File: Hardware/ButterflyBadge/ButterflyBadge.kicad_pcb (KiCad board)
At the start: 4 copper layers, 26.7 x 96.5 mm, 98 parts, among them J1 USB_C_Receptacle_USB2.0, J4 Conn_02x07_Odd_Even, M1 Motor_DC, P1 TC2030-CTX, Q1 ALS-PT19, Q2 Q_NMOS_GSD, SW1 SW_Push, SW3 SW_SPDT, U1 W25Q128JVS, U2 CN3058, U25 AP3722AT, U3 RP2040, U4 AX5201, U5 AMS1117-3.3, U6 Si24R1, U7 TFDU4301, U8 SM351LT, U9 TMI8118, Y1 12MHz, Y2 16MHz

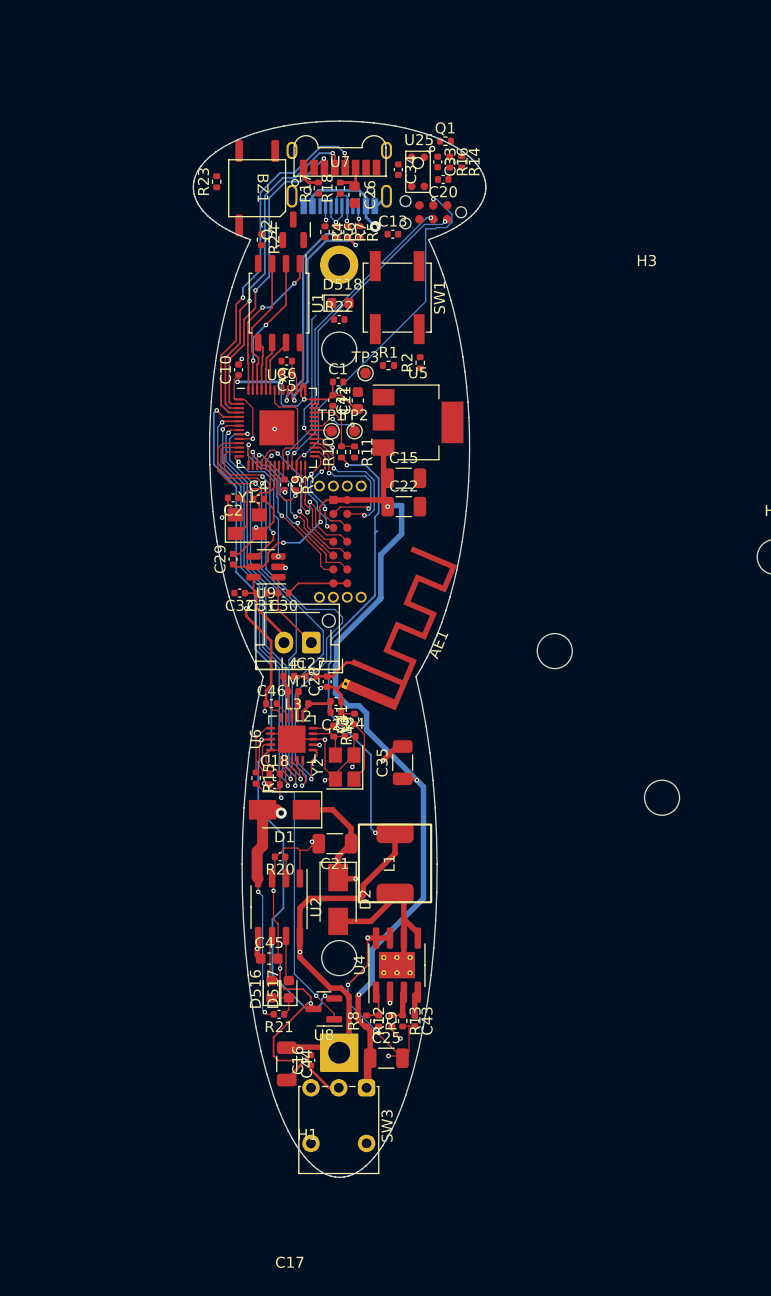
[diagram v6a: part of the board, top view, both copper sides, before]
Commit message: Routing done, next is error checking and assembly
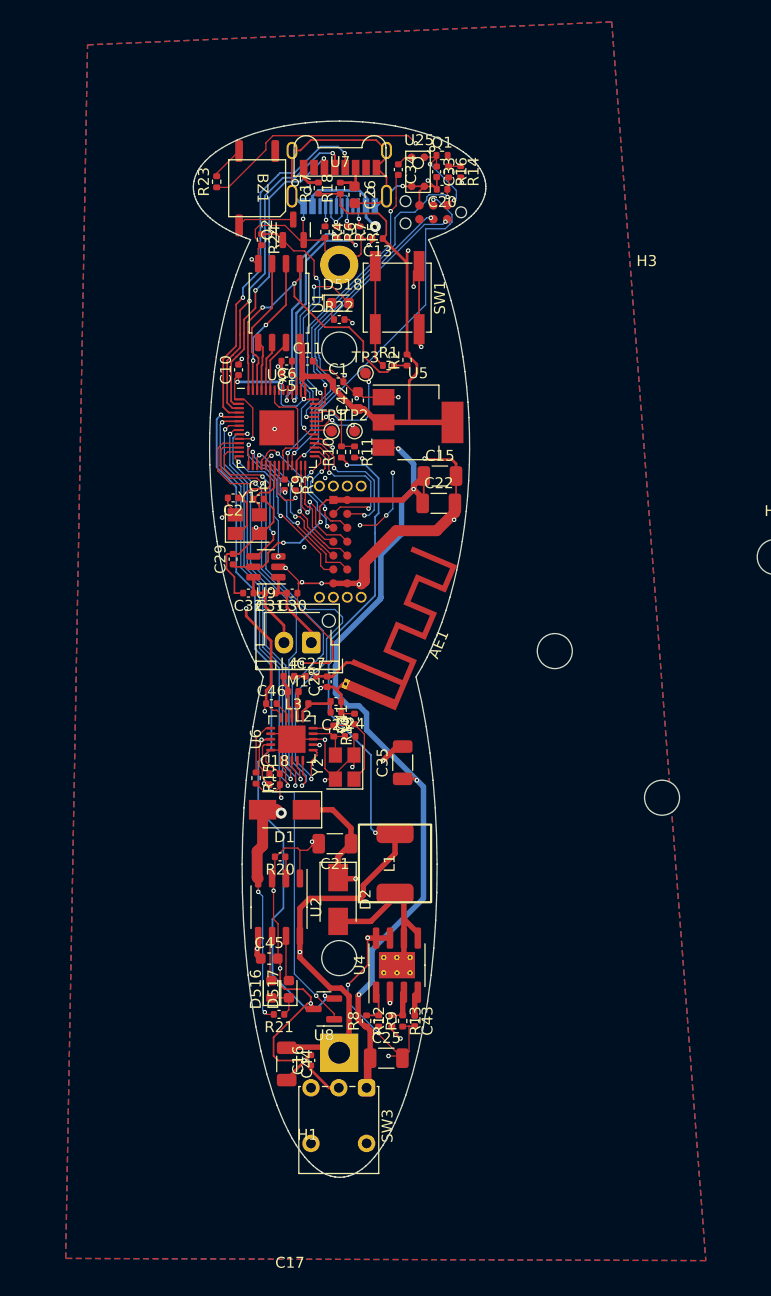
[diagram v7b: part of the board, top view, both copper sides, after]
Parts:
- moved C11 4.27 mm to (192.4, 68.8), turned to 0 degrees
- moved C15 3.31 mm to (204.5, 79.3)
- moved C22 3.21 mm to (204.4, 81.8)
- moved C13 1.46 mm to (198.8, 57.6), turned to 180 degrees
- moved Q1 1.33 mm to (204.7, 50.0)
- moved R2 1.23 mm to (201.5, 68.7)
- moved C20 0.91 mm to (204.7, 53.1)
- moved C33 0.91 mm to (204.2, 51.5)
- moved R14 0.91 mm to (206.4, 51.5)
- moved R16 0.91 mm to (205.3, 51.5)
- moved C30 0.80 mm to (191.0, 90.0)
- moved C31 0.80 mm to (189.0, 90.0)
- moved C32 0.80 mm to (187.0, 90.0)
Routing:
- net GND: track 131.5 -> 359.8 mm, vias 23 -> 48
- net +5V: track 92.6 -> 154.9 mm, vias 5 -> 7
- net +3V3: track 125.4 -> 183.1 mm, vias 12 -> 15
- net /AMBIENT_LIGHT: track 0.00 -> 29.6 mm, vias 0 -> 2
- net /MIC_OUT: track 0.00 -> 25.5 mm, vias 0 -> 2
- net /BUZZER: track 0.00 -> 22.3 mm, vias 0 -> 2
- net Net-(U1-~{CS}): track 14.0 -> 29.4 mm
- net Net-(U3-GPIO25): track 0.00 -> 9.61 mm, vias 0 -> 2
- net Net-(R1-Pad1): track 0.00 -> 9.37 mm
- net /LED: track 12.0 -> 19.3 mm, vias 1 -> 2
- net Net-(BZ1-+): track 0.00 -> 5.17 mm
- net Net-(BZ1--): track 0.00 -> 3.15 mm
- net Net-(Q1-E): track 0.00 -> 2.13 mm
- net Net-(D518-K): track 0.00 -> 1.59 mm
- net Net-(U25-OUT): track 0.00 -> 1.49 mm
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- added copper zone on B.Cu, net GND
- added copper zone on F.Cu, net GND
- added copper zone on In1.Cu, net GND
- added copper zone on In2.Cu, net GND

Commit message: Commit before changing board outline
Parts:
- removed H1, H2, H3: , MountingHole:MountingHole_3.2mm_M3
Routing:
- net GND: track 359.8 -> 454.2 mm, vias 48 -> 51
- net /SCK: track 38.1 -> 39.1 mm
- net /CIPO: track 42.8 -> 43.5 mm
